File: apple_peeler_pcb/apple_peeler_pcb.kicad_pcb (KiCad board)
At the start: 2 copper layers, 103 parts, among them J1 BM03B-SRSS-TB, J2 BM03B-SRSS-TB, J3 HYC10-HDMIA19-600B, J4 HYC10-HDMIA19-600B, J5 USB_C_Receptacle_USB2.0_16P, Q1 2N7002, Q10 2N7002, Q11 2N7002, Q12 2N7002, Q13 2N7002, Q2 2N7002, Q3 2N7002, Q4 2N7002, Q5 2N7002, Q6 2N7002, Q7 2N7002, Q8 AO3401A, Q9 2N7002, SW1 SPST BTN, SW2 SPST BTN, U1 W25Q16JVSS, U2 RP2040, U3 4066, U4 TPS562242, Y1 12MHz

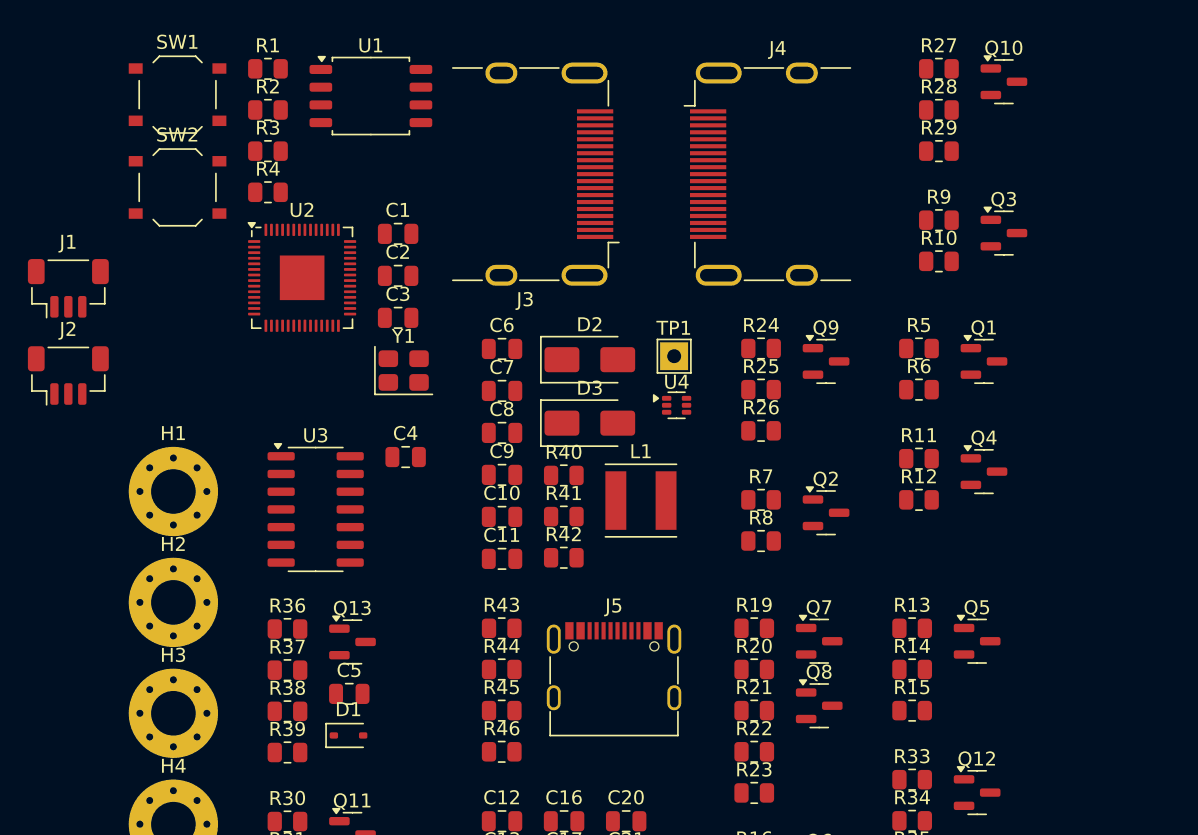
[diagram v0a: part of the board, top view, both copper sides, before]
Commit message: add some leds
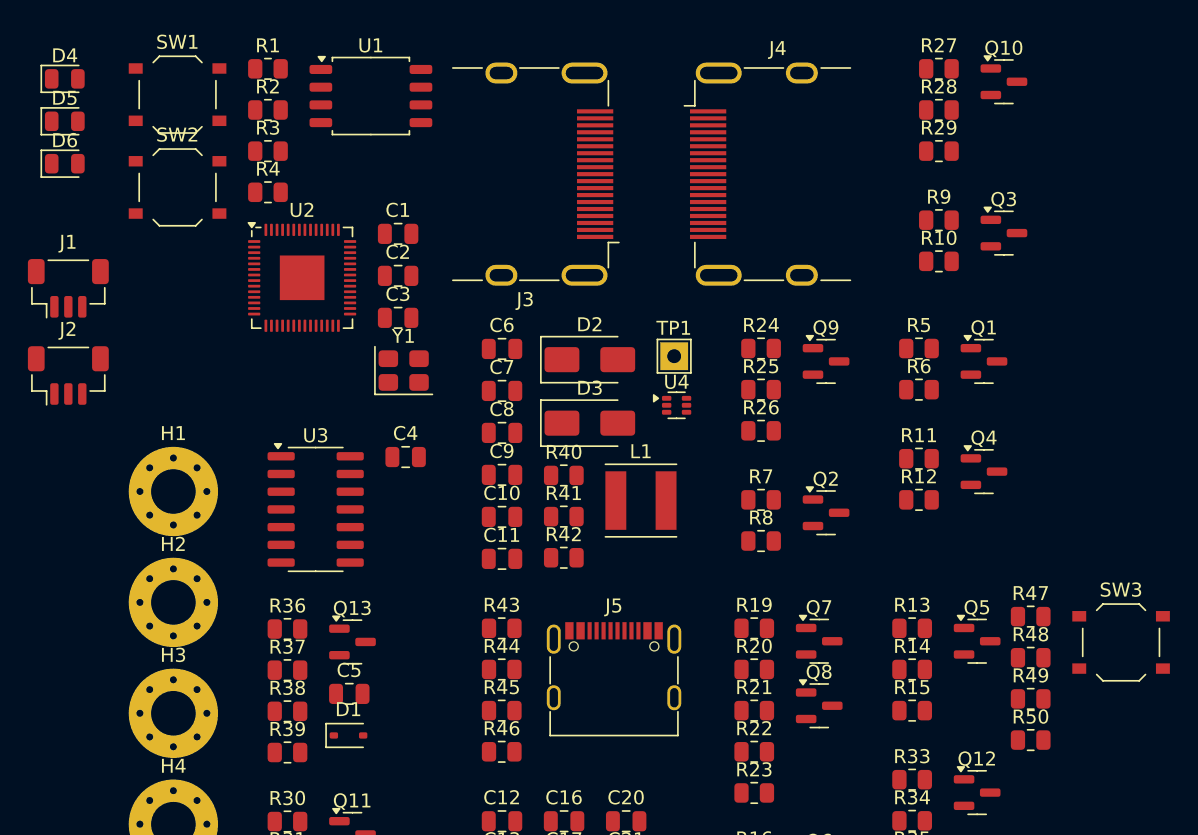
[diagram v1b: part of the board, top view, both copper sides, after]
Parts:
- added D4: GREEN, LED_SMD:LED_0805_2012Metric, F.Cu at (57.8, 35.5)
- added D5: YELLOW, LED_SMD:LED_0805_2012Metric, F.Cu at (57.8, 38.6)
- added D6: RED, LED_SMD:LED_0805_2012Metric, F.Cu at (57.8, 41.6)
- added R47: 1kΩ, Resistor_SMD:R_0805_2012Metric, F.Cu at (127.0, 74.1)
- added R48: 1kΩ, Resistor_SMD:R_0805_2012Metric, F.Cu at (127.0, 77.0)
- added R49: 1kΩ, Resistor_SMD:R_0805_2012Metric, F.Cu at (127.0, 80.0)
- added R50: 10kΩ, Resistor_SMD:R_0805_2012Metric, F.Cu at (127.0, 82.9)
- added SW3: SPST BTN, Button_Switch_SMD:SW_Push_1P1T_XKB_TS-1187A, F.Cu at (133.5, 75.9)
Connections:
- U2 pad 11: unconnected-(U2-GPIO8-Pad11) -> /HDMI passthrough/VCC_MON
- U2 pad 12: /HDMI passthrough/SDA_SRC_3V3 -> unconnected-(U2-GPIO9-Pad12)
- U2 pad 13: /HDMI passthrough/SDA_SINK_3V3 -> /HDMI passthrough/SDA_SRC_3V3
- U2 pad 14: /HDMI passthrough/SDA_BRIDGE -> /HDMI passthrough/SDA_SINK_3V3
- U2 pad 15: unconnected-(U2-GPIO12-Pad15) -> /HDMI passthrough/SDA_BRIDGE
- U2 pad 16: /HDMI passthrough/SCL_SRC_3V3 -> unconnected-(U2-GPIO13-Pad16)
- U2 pad 17: /HDMI passthrough/SCL_SINK_3V3 -> /HDMI passthrough/SCL_SRC_3V3
- U2 pad 18: /HDMI passthrough/SCL_BRIDGE -> /HDMI passthrough/SCL_SINK_3V3
- U2 pad 27: unconnected-(U2-GPIO16-Pad27) -> /HDMI passthrough/SCL_BRIDGE
- U2 pad 28: /HDMI passthrough/HPD_SRC_ASSERT -> unconnected-(U2-GPIO17-Pad28)
- U2 pad 29: /HDMI passthrough/HPD_SINK_MON -> /HDMI passthrough/HPD_SRC_ASSERT
- U2 pad 30: unconnected-(U2-GPIO19-Pad30) -> /HDMI passthrough/HPD_SINK_MON
- U2 pad 31: /HDMI passthrough/HPD_ARC_BRIDGE -> unconnected-(U2-GPIO20-Pad31)
- U2 pad 32: unconnected-(U2-GPIO21-Pad32) -> /HDMI passthrough/HPD_ARC_BRIDGE
- U2 pad 34: /HDMI passthrough/CEC_MON -> unconnected-(U2-GPIO22-Pad34)
- U2 pad 35: /HDMI passthrough/CEC_BRIDGE -> /HDMI passthrough/CEC_MON
- U2 pad 36: /HDMI passthrough/CEC_PULLDOWN -> /HDMI passthrough/CEC_BRIDGE
- U2 pad 37: unconnected-(U2-GPIO25-Pad37) -> /HDMI passthrough/CEC_PULLDOWN
- U2 pad 5: unconnected-(U2-GPIO3-Pad5) -> /UI/USR_BTN
- U2 pad 6: unconnected-(U2-GPIO4-Pad6) -> /UI/GREEN_LED
- U2 pad 7: unconnected-(U2-GPIO5-Pad7) -> /UI/RED_LED
- U2 pad 8: unconnected-(U2-GPIO6-Pad8) -> /UI/YELLOW_LED
- U2 pad 9: /HDMI passthrough/VCC_MON -> unconnected-(U2-GPIO7-Pad9)

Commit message: add power led
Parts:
- added D7: GREEN, LED_SMD:LED_0805_2012Metric, F.Cu at (64.7, 51.9)
- added R50: 1kΩ, Resistor_SMD:R_0805_2012Metric, F.Cu at (64.7, 54.9)
- renumbered R50 to R51

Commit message: some progress
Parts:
- removed C20: 100nF, Capacitor_SMD:C_0805_2012Metric
- removed the D4 at (57.8, 35.5)
- removed the Q10 at (125.1, 35.7)
- removed the Q7 at (111.9, 75.8)
- removed the R19 at (107.2, 74.9)
- removed the R20 at (107.2, 77.9)
- removed the R21 at (107.2, 80.8)
- removed the R27 at (120.5, 34.8)
- removed the R28 at (120.5, 37.7)
- removed the R29 at (120.5, 40.7)
- added C24: 100pF, Capacitor_SMD:C_0805_2012Metric, F.Cu at (149.1, 39.1)
- added D7: 1N4148WS, Diode_SMD:D_SOD-323, F.Cu at (149.1, 42.1)
- added Q12: 2N7002, Package_TO_SOT_SMD:SOT-23, F.Cu at (149.3, 60.1)
- added Q13: 2N7002, Package_TO_SOT_SMD:SOT-23, F.Cu at (138.0, 52.2)
- added Q14: AO3401A, Package_TO_SOT_SMD:SOT-23, F.Cu at (138.0, 56.8)
- added Q15: 2N7002, Package_TO_SOT_SMD:SOT-23, F.Cu at (138.0, 35.4)
- added Q16: AO3401A, Package_TO_SOT_SMD:SOT-23, F.Cu at (138.0, 40.0)
- added Q17: 2N7002, Package_TO_SOT_SMD:SOT-23, F.Cu at (149.3, 35.4)
- added Q18: 2N7002, Package_TO_SOT_SMD:SOT-23, F.Cu at (160.7, 49.2)
- added R24: 10kΩ, Resistor_SMD:R_0805_2012Metric, F.Cu at (144.7, 54.2)
- added R44: 510Ω, Resistor_SMD:R_0805_2012Metric, F.Cu at (144.7, 59.1)
- added R45: 470kΩ, Resistor_SMD:R_0805_2012Metric, F.Cu at (144.7, 62.1)
- added R46: 10kΩ, Resistor_SMD:R_0805_2012Metric, F.Cu at (144.7, 65.0)
- added R50: 510Ω, Resistor_SMD:R_0805_2012Metric, F.Cu at (133.4, 60.1)
- added R51: 470kΩ, Resistor_SMD:R_0805_2012Metric, F.Cu at (133.4, 63.0)
- added R52: 510Ω, Resistor_SMD:R_0805_2012Metric, F.Cu at (133.4, 34.5)
- added R53: 470kΩ, Resistor_SMD:R_0805_2012Metric, F.Cu at (133.4, 37.4)
- added R54: 10kΩ, Resistor_SMD:R_0805_2012Metric, F.Cu at (133.4, 40.4)
- added R55: 510Ω, Resistor_SMD:R_0805_2012Metric, F.Cu at (133.4, 43.3)
- added R56: 470kΩ, Resistor_SMD:R_0805_2012Metric, F.Cu at (133.4, 46.3)
- added R57: 510Ω, Resistor_SMD:R_0805_2012Metric, F.Cu at (144.7, 34.5)
- added R58: 470kΩ, Resistor_SMD:R_0805_2012Metric, F.Cu at (144.7, 37.4)
- added R59: 27kΩ, Resistor_SMD:R_0805_2012Metric, F.Cu at (144.7, 40.4)
- added R60: 47kΩ, Resistor_SMD:R_0805_2012Metric, F.Cu at (144.7, 43.3)
- added R61: 510Ω, Resistor_SMD:R_0805_2012Metric, F.Cu at (156.0, 48.3)
- added R62: 470kΩ, Resistor_SMD:R_0805_2012Metric, F.Cu at (156.0, 51.2)
- added R63: 10kΩ, Resistor_SMD:R_0805_2012Metric, F.Cu at (156.0, 54.2)
- D5: value YELLOW -> SK6812MINI; footprint LED_SMD:LED_0805_2012Metric -> LED_SMD:LED_SK6812MINI_PLCC4_3.5x3.5mm_P1.75mm
- D6: value RED -> SK6812MINI; footprint LED_SMD:LED_0805_2012Metric -> LED_SMD:LED_SK6812MINI_PLCC4_3.5x3.5mm_P1.75mm
- Q8: value AO3401A -> 2N7002
- R47: value 1kΩ -> 510Ω
- R48: value 1kΩ -> 470kΩ
- R49: value 1kΩ -> 10kΩ
- moved U2 189.3 mm to (190.3, 199.8), turned to 90 degrees
- moved C3 171.9 mm to (180.8, 193.0), turned to 180 degrees
- moved C21 149.9 mm to (191.3, 209.0), turned to -90 degrees
- moved C22 147.4 mm to (201.6, 199.6)
- moved TP1 147.3 mm to (179.7, 180.3)
- moved C18 147.0 mm to (186.1, 209.0), turned to -90 degrees
- moved R37 146.2 mm to (180.6, 187.3)
- moved C7 145.4 mm to (165.1, 181.9), turned to -90 degrees
- moved C9 143.7 mm to (176.8, 177.7), turned to 90 degrees
- moved C6 143.6 mm to (165.1, 176.8), turned to 90 degrees
- moved C10 143.6 mm to (174.3, 182.5), turned to -90 degrees
- moved R38 143.4 mm to (166.3, 195.7)
- moved C8 143.1 mm to (171.7, 177.7), turned to -90 degrees
- moved C11 142.7 mm to (176.8, 182.5), turned to -90 degrees
- moved R35 139.5 mm to (174.3, 177.7), turned to 90 degrees
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- renumbered D7 to D4, Q12 to Q10, Q13 to Q11, Q9 to Q7, Q11 to Q9, R24 to R19, R25 to R20, R26 to R21, R30 to R25, R31 to R26, R32 to R27, R33 to R28, R34 to R29, R35 to R30, R36 to R31, R37 to R32, R38 to R33, R39 to R34, R40 to R35, R41 to R36, R42 to R37, R43 to R38, R44 to R39, R45 to R40, R46 to R41, R50 to R42, R51 to R43
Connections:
- net /HDMI passthrough/HDMI connectors/CEC_SINK renamed /HDMI passthrough/CEC interface1/CEC_LINE
- net /USB/DM renamed /USB/DN
- C5 pad 1: /HDMI passthrough/CEC_MON -> /HDMI passthrough/CEC_SRC_MON
- D5 pad 1: GND -> Net-(D5-DOUT)
- D5 pad 2: Net-(D5-A) -> GND
- D6 pad 1: GND -> unconnected-(D6-DOUT-Pad1)
- D6 pad 2: Net-(D6-A) -> GND
- Q8 pad 2: +5V -> GND
- Q8 pad 3: /HDMI passthrough/HDMI connectors/HPD_SRC -> /HDMI passthrough/HPD_SINK_MON
- R22 pad 1: Net-(Q8-G) -> /HDMI passthrough/HDMI connectors/HPD_SINK
- R22 pad 2: Net-(Q7-D) -> Net-(Q8-G)
- R23 pad 1: /HDMI passthrough/HDMI connectors/HPD_SRC -> Net-(Q8-G)
- R31 pad 1: /HDMI passthrough/CEC_PULLDOWN -> /HDMI passthrough/CEC_SRC_PULLDOWN
- R34 pad 2: /HDMI passthrough/CEC_MON -> /HDMI passthrough/CEC_SRC_MON
- R47 pad 1: Net-(D4-A) (its old number) -> /HDMI passthrough/HPD_SRC_ASSERT
- R47 pad 2: /UI/GREEN_LED -> Net-(Q13-G)
- R48 pad 1: Net-(D5-A) -> Net-(Q13-G)
- R48 pad 2: /UI/YELLOW_LED -> GND
- R49 pad 1: Net-(D6-A) -> +5V
- R49 pad 2: /UI/RED_LED -> Net-(Q14-G)
- U2 pad 14: /HDMI passthrough/SDA_SINK_3V3 -> /HDMI passthrough/SCL_SRC_3V3
- U2 pad 15: /HDMI passthrough/SDA_BRIDGE -> /HDMI passthrough/SDA_SINK_3V3
- U2 pad 16: unconnected-(U2-GPIO13-Pad16) -> /HDMI passthrough/SCL_SINK_3V3
- U2 pad 17: /HDMI passthrough/SCL_SRC_3V3 -> /HDMI passthrough/SDA_BRIDGE
- U2 pad 18: /HDMI passthrough/SCL_SINK_3V3 -> /HDMI passthrough/SCL_BRIDGE
- U2 pad 27: /HDMI passthrough/SCL_BRIDGE -> /HDMI passthrough/HPD_SRC_MON
- U2 pad 28: unconnected-(U2-GPIO17-Pad28) -> /HDMI passthrough/HPD_SRC_ASSERT
- U2 pad 29: /HDMI passthrough/HPD_SRC_ASSERT -> /HDMI passthrough/HPD_SINK_MON
- U2 pad 30: /HDMI passthrough/HPD_SINK_MON -> /HDMI passthrough/HPD_SINK_ASSERT
- U2 pad 31: unconnected-(U2-GPIO20-Pad31) -> /HDMI passthrough/HPD_ARC_BRIDGE
- U2 pad 32: /HDMI passthrough/HPD_ARC_BRIDGE -> /HDMI passthrough/CEC_SINK_MON
- U2 pad 34: unconnected-(U2-GPIO22-Pad34) -> /HDMI passthrough/CEC_SINK_PULLDOWN
- U2 pad 35: /HDMI passthrough/CEC_MON -> /HDMI passthrough/CEC_SRC_PULLDOWN
- U2 pad 36: /HDMI passthrough/CEC_BRIDGE -> /HDMI passthrough/CEC_SRC_MON
- U2 pad 37: /HDMI passthrough/CEC_PULLDOWN -> /HDMI passthrough/CEC_BRIDGE
- U2 pad 6: /UI/GREEN_LED -> /UI/WLED
- U2 pad 7: /UI/RED_LED -> unconnected-(U2-GPIO5-Pad7)
- U2 pad 8: /UI/YELLOW_LED -> unconnected-(U2-GPIO6-Pad8)
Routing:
- net +3.3V: track 0.00 -> 50.1 mm
- net /HDMI passthrough/HDMI connectors/D1-: track 0.00 -> 31.1 mm, vias 0 -> 2
- net /HDMI passthrough/HDMI connectors/D2+: track 0.00 -> 30.3 mm, vias 0 -> 2
- net /HDMI passthrough/HDMI connectors/D2-: track 0.00 -> 30.2 mm, vias 0 -> 2
- net /HDMI passthrough/HDMI connectors/D1+: track 0.00 -> 30.1 mm, vias 0 -> 2
- net /HDMI passthrough/HDMI connectors/D0-: track 0.00 -> 30.1 mm, vias 0 -> 2
- net /HDMI passthrough/HDMI connectors/D0+: track 0.00 -> 30.0 mm, vias 0 -> 2
- net /HDMI passthrough/HDMI connectors/CK-: track 0.00 -> 29.9 mm, vias 0 -> 2
- net /HDMI passthrough/HDMI connectors/CK+: track 0.00 -> 29.6 mm, vias 0 -> 2
- net /HDMI passthrough/HDMI_VCC: track 0.00 -> 25.9 mm
- net /USB/DN: track 0.00 -> 25.3 mm
- net /USB/DP: track 0.00 -> 25.3 mm
- net GND: track 0.00 -> 24.6 mm, vias 0 -> 10
- net /Power supply/USB_VCC: track 0.00 -> 23.7 mm
- net /HDMI passthrough/HDMI connectors/HPD_SRC: track 0.00 -> 23.0 mm, vias 0 -> 2
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
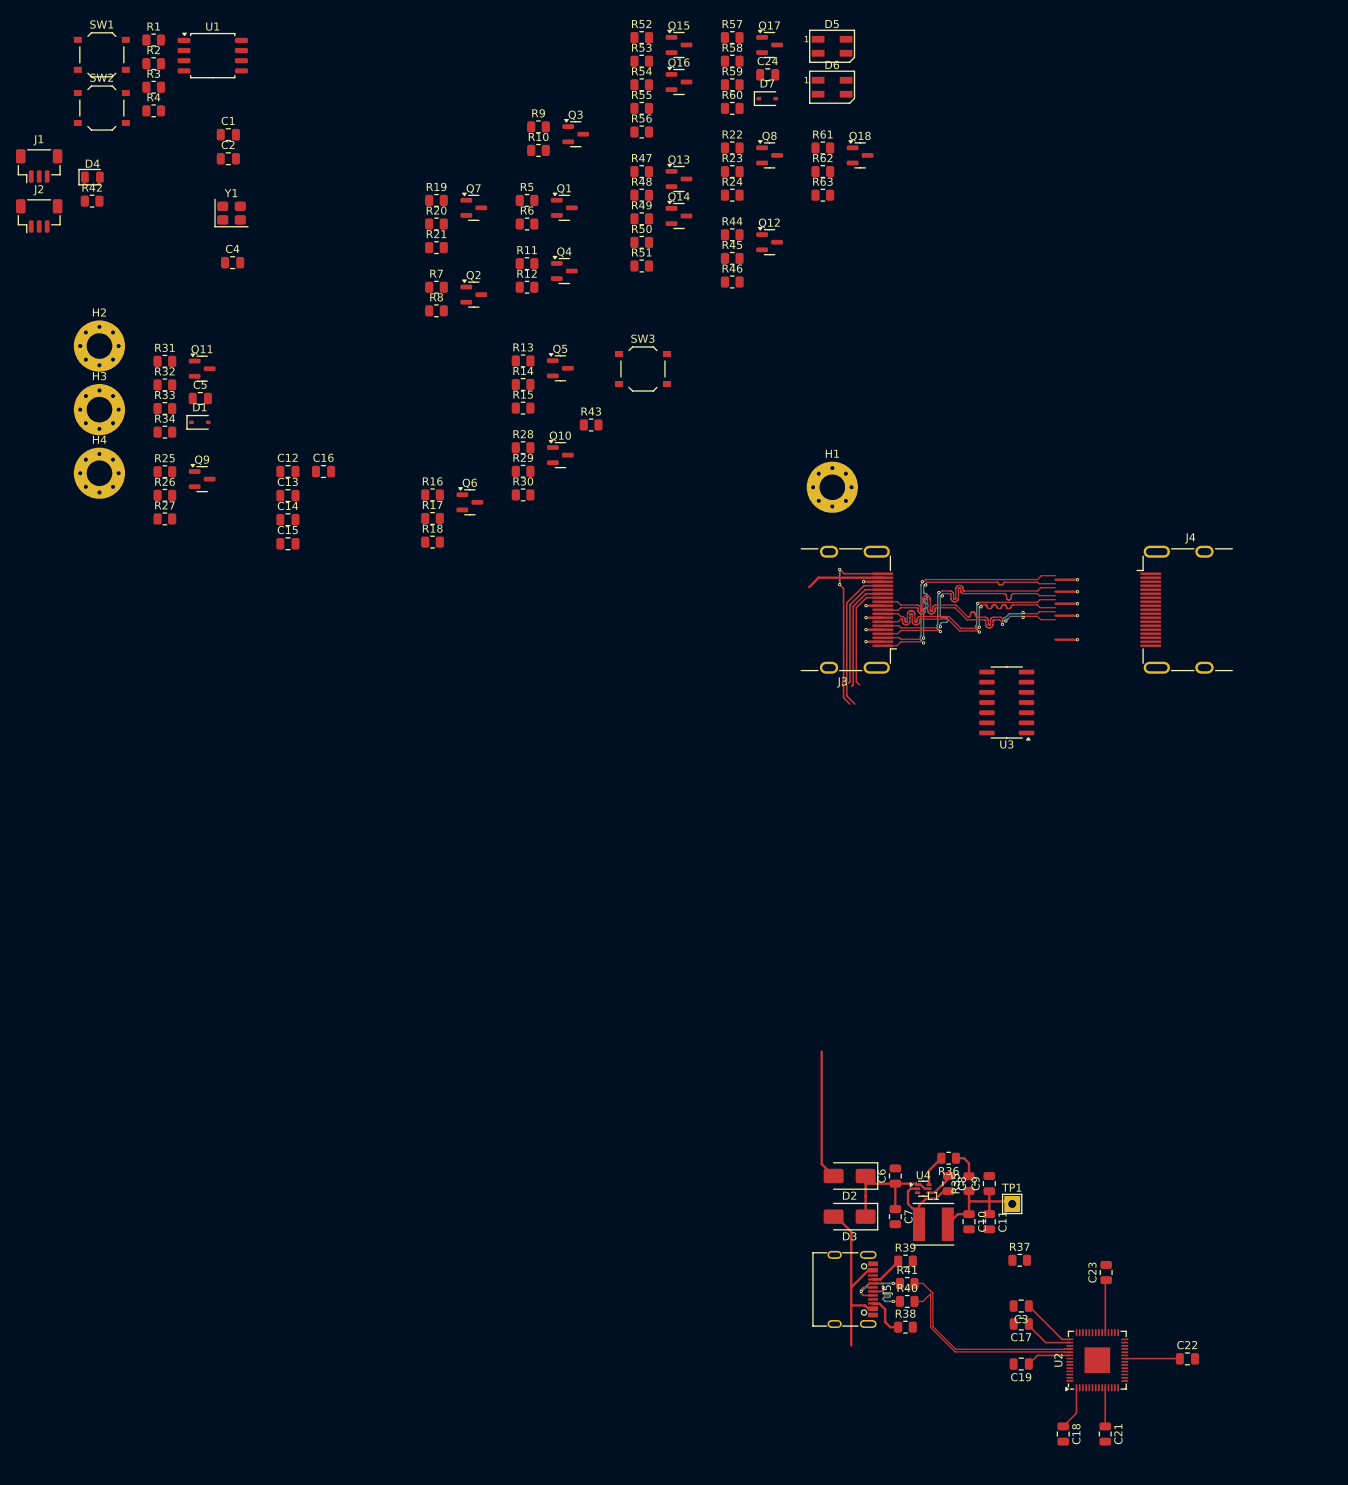
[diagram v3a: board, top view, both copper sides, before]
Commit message: route and place MCU peripherals and power train
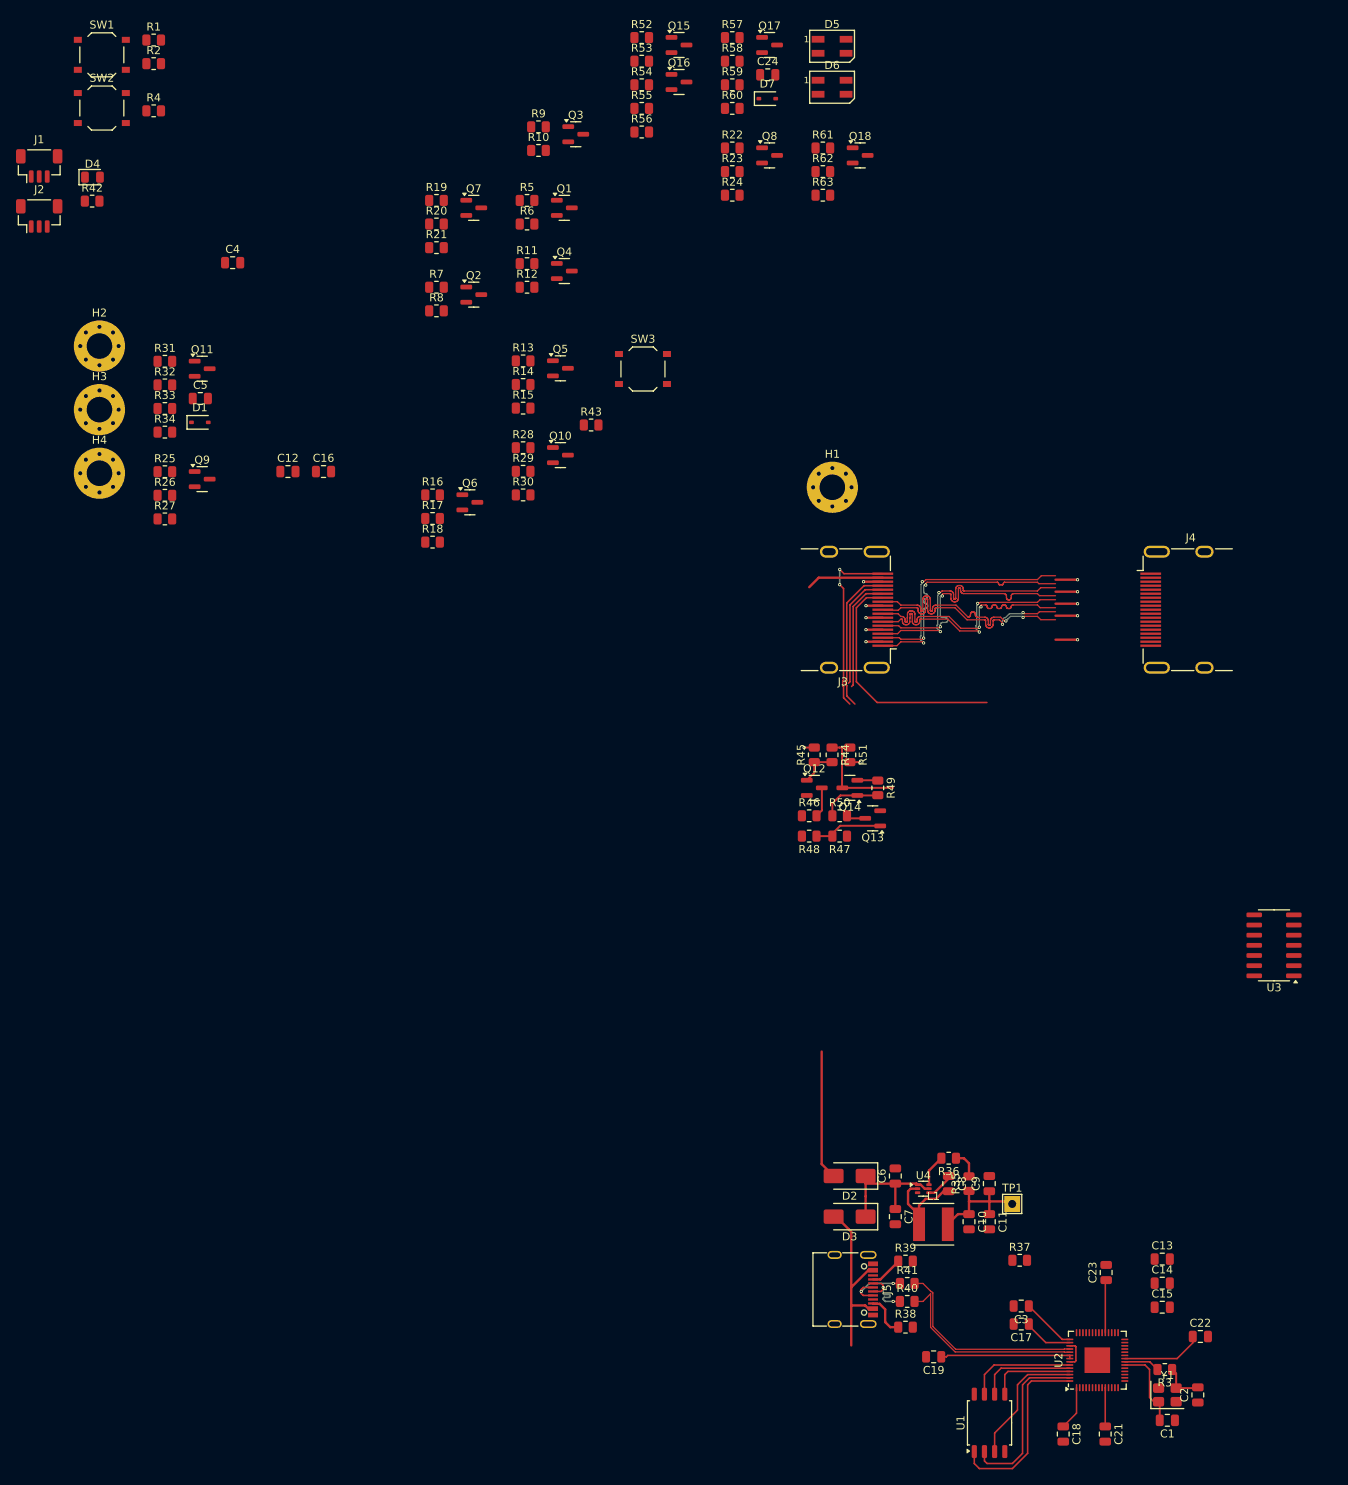
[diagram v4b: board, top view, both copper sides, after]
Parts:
- moved R3 204.1 mm to (198.8, 201.0), turned to 180 degrees
- moved C1 199.0 mm to (199.1, 207.3), turned to 180 degrees
- moved U1 196.6 mm to (176.8, 207.6), turned to 90 degrees
- moved C2 196.4 mm to (202.9, 204.2), turned to 90 degrees
- moved Y1 188.4 mm to (199.1, 204.2)
- moved C13 145.1 mm to (198.4, 187.2)
- moved C14 145.1 mm to (198.4, 190.2)
- moved C15 145.1 mm to (198.4, 193.2)
- moved R47 86.7 mm to (158.1, 134.3), turned to 180 degrees
- moved Q13 83.5 mm to (162.2, 132.1), turned to 180 degrees
- moved R48 82.8 mm to (154.3, 134.3), turned to 180 degrees
- moved R49 77.0 mm to (162.9, 128.3), turned to -90 degrees
- moved R50 75.8 mm to (158.1, 131.8)
- moved Q14 74.6 mm to (159.4, 128.3), turned to 180 degrees
- moved Q12 68.4 mm to (154.9, 128.3)
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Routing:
- net /FLASH_CS: track 0.00 -> 23.3 mm
- net /FLASH_D1: track 0.00 -> 21.4 mm
- net /HDMI passthrough/CEC interface/CEC_LINE: track 13.6 -> 30.5 mm
- net /FLASH_D2: track 0.00 -> 16.6 mm
- net +3.3V: track 50.1 -> 64.3 mm
- net /HDMI passthrough/HDMI connectors/HPD_SRC: track 23.0 -> 36.7 mm
- net /FLASH_D3: track 0.00 -> 13.6 mm
- net /FLASH_CLK: track 0.00 -> 12.2 mm
- net /FLASH_D0: track 0.00 -> 10.7 mm
- net Net-(U2-XIN): track 0.00 -> 10.5 mm
- net Net-(Q13-G): track 0.00 -> 8.69 mm
- net Net-(Q14-G): track 0.00 -> 7.65 mm
- net Net-(C2-Pad2): track 0.00 -> 5.29 mm
- net Net-(Q12-G): track 0.00 -> 4.88 mm
- net Net-(U2-XOUT): track 0.00 -> 4.48 mm
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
